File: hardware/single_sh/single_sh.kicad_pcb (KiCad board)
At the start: 4 copper layers, 122 x 20 mm, 151 parts, among them J1 USB-C, J11 M1+M2, J12 M3+M4, J13 M5+M6, J14 M7+M8, J15 M9+M10, J2 Qwiic, J3 Qwiic, J4 5V IN, J5 LED STRIP, J6 LED PWR, J7 E-STOP, J8 PANEL BTN, Q1 AO3401A, SW1 BTN1, SW2 BTN2, SW3 BOOTSEL, U1 AT8833CQ, U10 AT8833CQ, U11 RP2354B, U12 TPD2E2U06, U13 ME6211C33M5G, U14 74AHCT1G125, U15 74AHCT1G125, U2 AT8833CQ, U3 AT8833CQ, U4 AT8833CQ, U5 AT8833CQ, U6 AT8833CQ, U7 AT8833CQ, U8 AT8833CQ, U9 AT8833CQ, Y1 12MHz

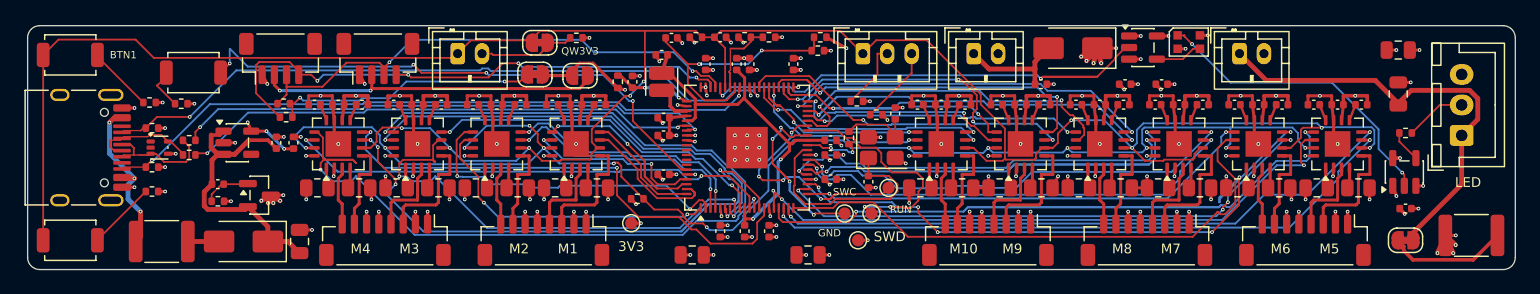
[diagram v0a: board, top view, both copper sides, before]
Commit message: PCB route cleanup
A few human reroutes
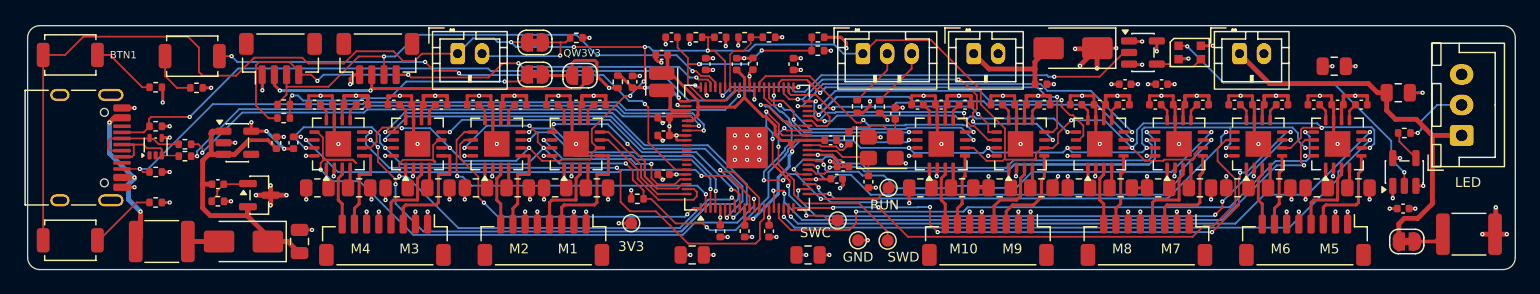
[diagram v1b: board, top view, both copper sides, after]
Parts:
- moved C31 5.41 mm to (146.2, 93.3)
- moved TP2 2.59 mm to (109.5, 107.6)
- moved R36 1.80 mm to (52.9, 95.1)
- moved C38 1.40 mm to (105.9, 101.5), turned to 180 degrees
- moved SW3 1.35 mm to (52.5, 92.5)
- moved R34 1.35 mm to (49.5, 95.0)
- moved R26 1.35 mm to (51.9, 100.7)
- moved R35 0.95 mm to (49.5, 104.5)
- moved R27 0.94 mm to (51.9, 99.7)
- moved D2 0.86 mm to (134.3, 92.2)
- moved TP1 0.81 mm to (105.4, 106.0)
- moved R41 0.71 mm to (108.9, 96.7), turned to -90 degrees
- moved C37 0.50 mm to (105.3, 102.5)
- moved R29 0.50 mm to (49.5, 102.0)
- moved R40 0.43 mm to (107.0, 96.6), turned to -90 degrees
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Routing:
- net M5_AIN2: track 71.2 -> 51.2 mm
- net /MCU/XIN: track 18.2 -> 6.74 mm
- net /Connectors and UI/STRIP_V5_FUSED: track 9.91 -> 2.57 mm
- net LADDER: track 198.0 -> 203.5 mm, vias 9 -> 13
- net GND: track 122.0 -> 127.2 mm
- net +3V3: track 34.0 -> 39.1 mm, vias 28 -> 21
- net LED_DIN: track 41.0 -> 36.0 mm
- net M9_AIN2: track 24.9 -> 19.9 mm
- net M6_BIN2: track 52.5 -> 47.9 mm
- net /MCU/RUN: track 21.0 -> 25.2 mm
- net /Connectors and UI/STRIP_5V: track 35.9 -> 33.0 mm
- net /Power/V5_IN: track 23.5 -> 26.3 mm
- net USB_DM_MCU: track 42.5 -> 45.3 mm
- net USB_DP_MCU: track 44.1 -> 46.5 mm
- net Net-(J7-Pin_2): track 8.02 -> 10.0 mm, vias 0 -> 1
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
